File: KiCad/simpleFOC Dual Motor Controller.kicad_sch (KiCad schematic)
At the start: 15 parts, among them J101 Conn_01x04, U101 STM32F103C8Tx, U102 XT60H-M

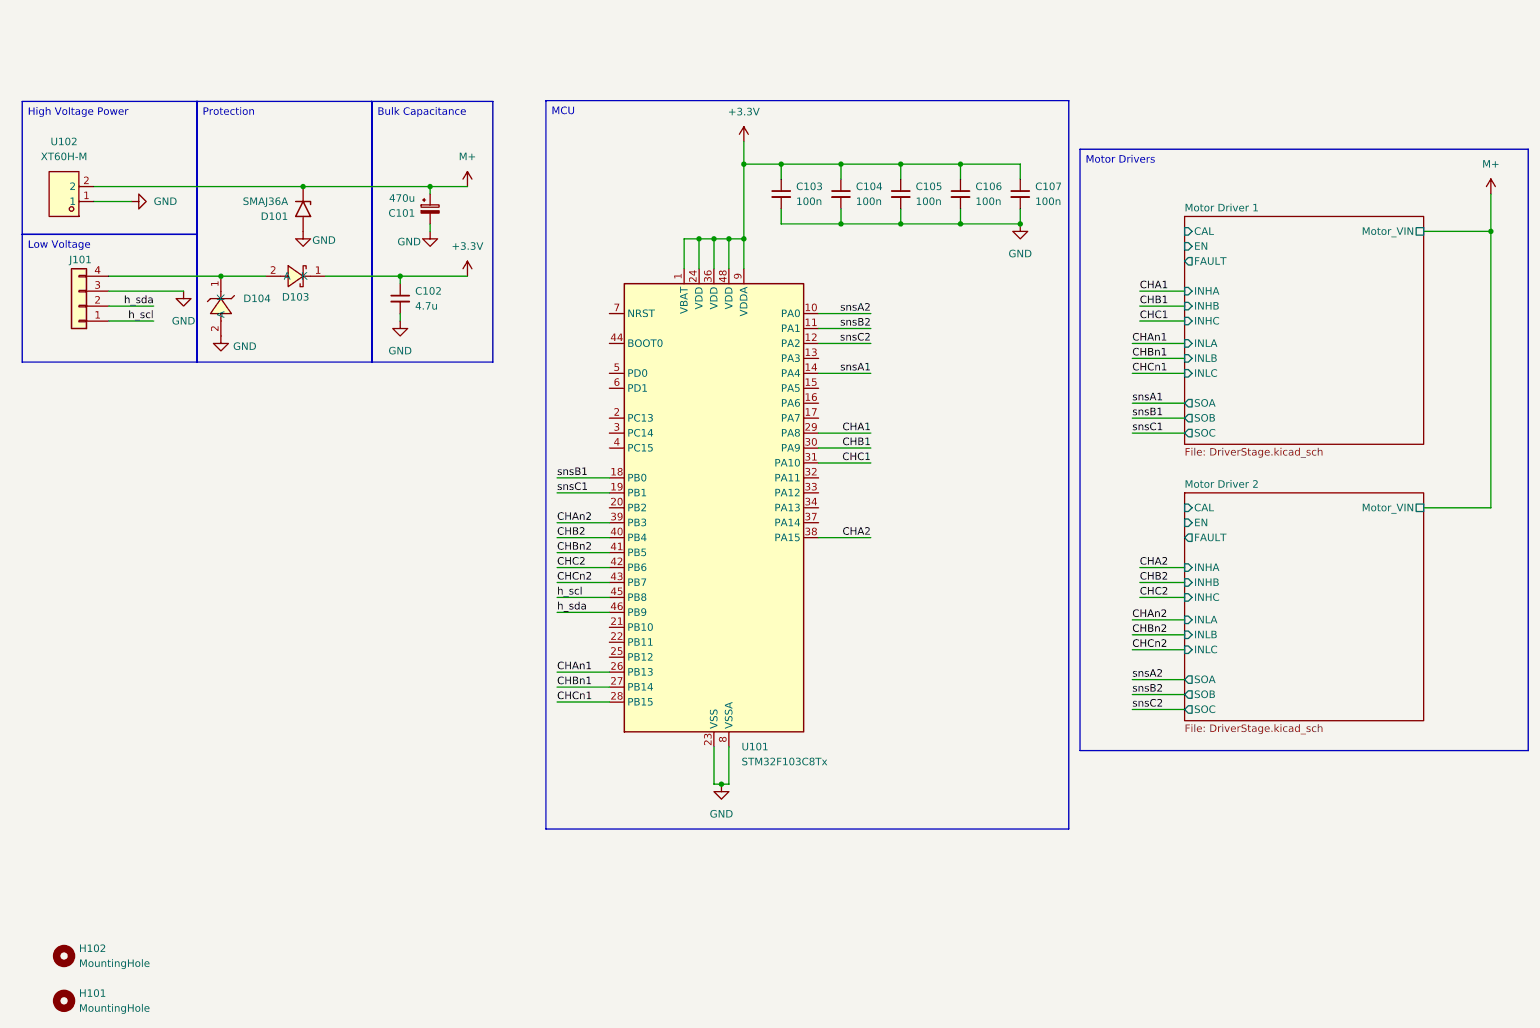
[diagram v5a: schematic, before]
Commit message: connected all control pins
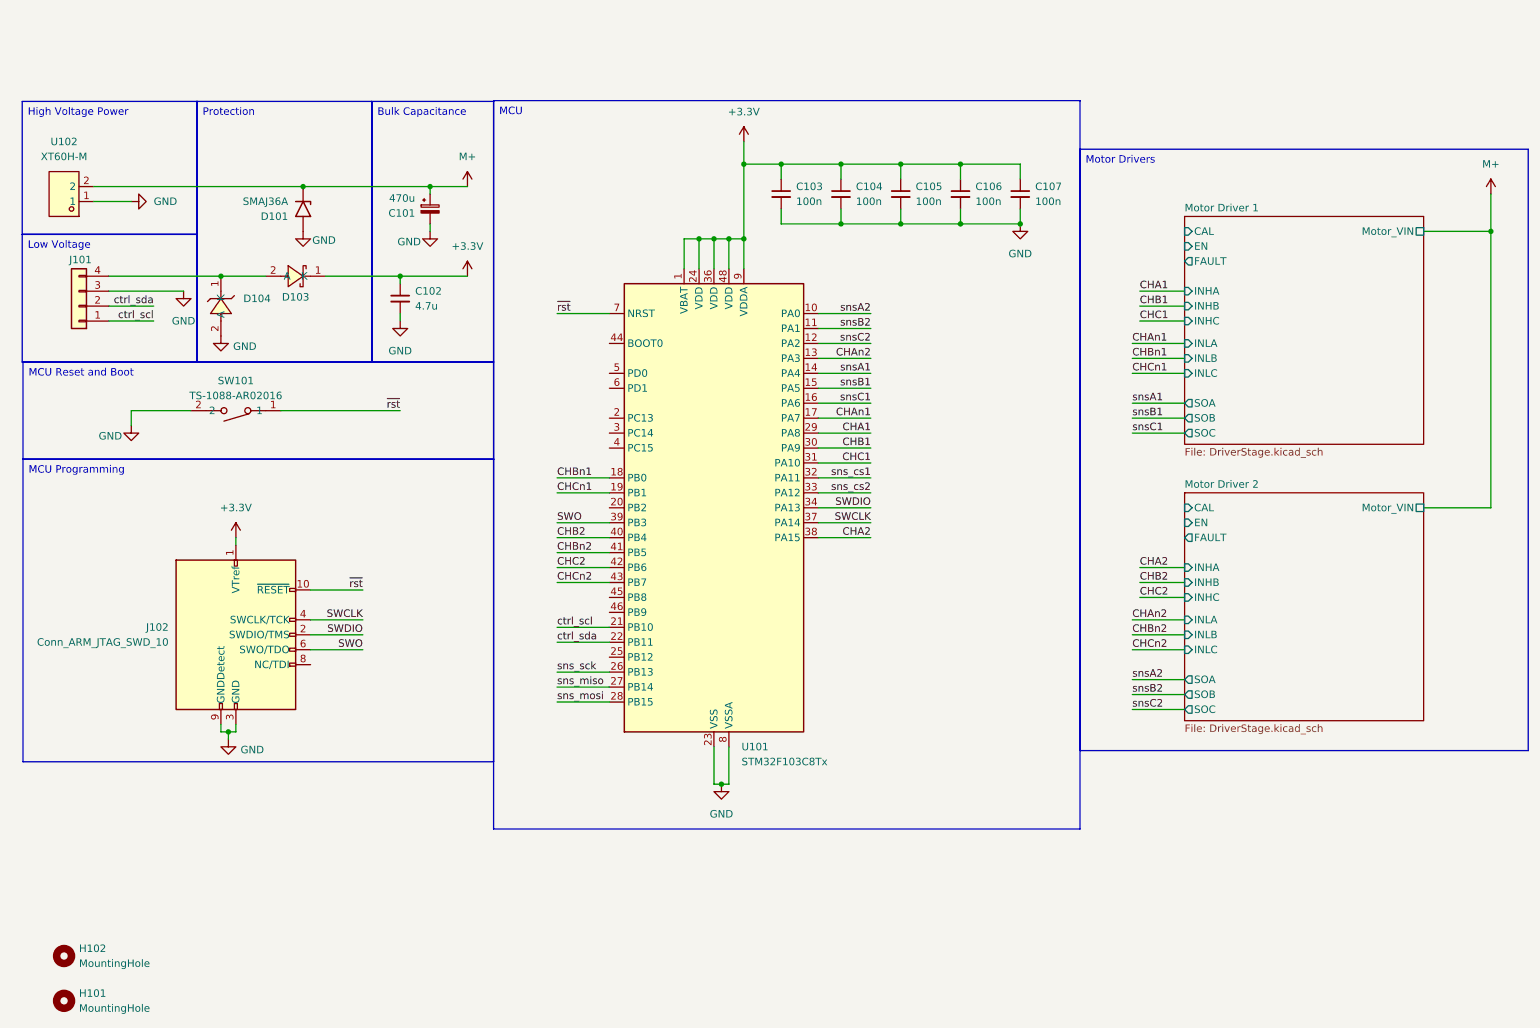
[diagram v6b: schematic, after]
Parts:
- added J102: Conn_ARM_JTAG_SWD_10, symbol Connector:Conn_ARM_JTAG_SWD_10
- added SW101: TS-1088-AR02016, easyeda2kicad:SW-SMD_L3.9-W3.0-P4.45, symbol easyeda2kicad:TS-1088-AR02016
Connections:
- net +3.3V: now also J102.1 (VTref)
- net CHAn1: now also U101.17 (PA7); no longer U101.26 (PB13)
- net CHAn2: now also U101.13 (PA3); no longer U101.39 (PB3)
- net CHBn1: now also U101.18 (PB0); no longer U101.27 (PB14)
- net CHCn1: now also U101.19 (PB1); no longer U101.28 (PB15)
- net GND: now also J102.3 (GND), J102.5 (GND), J102.9 (GNDDetect), SW101.2
- net snsB1: now also U101.15 (PA5); no longer U101.18 (PB0)
- net snsC1: now also U101.16 (PA6); no longer U101.19 (PB1)
- net ctrl_scl: now reaches U101.21 (PB10)
- net ctrl_scl: now also J101.1 (Pin_1)
- net ctrl_sda: now reaches U101.22 (PB11)
- net ctrl_sda: now also J101.2 (Pin_2)
- net sns_cs1: now reaches U101.32 (PA11)
- net sns_cs2: now reaches U101.33 (PA12)
- net SWDIO: now reaches U101.34 (PA13)
- net SWDIO: now also J102.2 (SWDIO/TMS)
- net SWCLK: now reaches U101.37 (PA14)
- net SWCLK: now also J102.4 (SWCLK/TCK)
- net ~{rst}: now reaches U101.7 (NRST)
- net ~{rst}: now also J102.10 (~{RESET}), SW101.1
- net h_scl: no longer names the net of U101.45 (PB8)
- net h_scl: no longer J101.1 (Pin_1)
- net h_sda: no longer names the net of U101.46 (PB9)
- net h_sda: no longer J101.2 (Pin_2)
- new net SWO: J102.6 (SWO/TDO), U101.39 (PB3)
- new net sns_miso: U101.27 (PB14)
- new net sns_mosi: U101.28 (PB15)
- new net sns_sck: U101.26 (PB13)

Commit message: not sure why the schematic and pcb aren't syncing :(
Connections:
- net CHAn1: now also U101.19 (PB1); no longer U101.17 (PA7)
- net CHCn1: now also U101.17 (PA7); no longer U101.19 (PB1)
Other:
- moved on the sheet: J102
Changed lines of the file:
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@@
 	)
 	(junction
-		(at 52.07 140.97)
+		(at 55.88 137.16)
 		(diameter 0)
 		(color 0 0 0 0)
@@
 	(wire
 		(pts
-			(xy 66.04 124.46) (xy 74.93 124.46)
+			(xy 69.85 120.65) (xy 78.74 120.65)
 		)
 		(stroke
@@
 	(wire
 		(pts
+			(xy 161.29 87.63) (xy 152.4 87.63)
+		)
+		(stroke
+			(width 0)
+			(type default)
+		)
+	)
+	(wire
+		(pts
 			(xy 31.75 66.04) (xy 44.45 66.04)
 		)
@@
 	(wire
 		(pts
-			(xy 66.04 127) (xy 74.93 127)
+			(xy 69.85 123.19) (xy 78.74 123.19)
 		)
 		(stroke
@@
 	(wire
 		(pts
-			(xy 50.8 140.97) (xy 52.07 140.97)
+			(xy 54.61 137.16) (xy 55.88 137.16)
 		)
 		(stroke
@@
 	(wire
 		(pts
-			(xy 66.04 116.84) (xy 74.93 116.84)
+			(xy 69.85 113.03) (xy 78.74 113.03)
 		)
 		(stroke
@@
 	(wire
 		(pts
-			(xy 53.34 139.7) (xy 53.34 140.97)
+			(xy 57.15 135.89) (xy 57.15 137.16)
 		)
 		(stroke
@@
 	(wire
 		(pts
-			(xy 66.04 121.92) (xy 74.93 121.92)
+			(xy 69.85 118.11) (xy 78.74 118.11)
 		)
 		(stroke
@@
 	(wire
 		(pts
-			(xy 161.29 87.63) (xy 152.4 87.63)
-		)
-		(stroke
-			(width 0)
-			(type default)
-		)
-	)
-	(wire
-		(pts
 			(xy 152.4 77.47) (xy 161.29 77.47)
 		)
@@
 	(wire
 		(pts
-			(xy 53.34 140.97) (xy 52.07 140.97)
+			(xy 57.15 137.16) (xy 55.88 137.16)
 		)
 		(stroke
@@
 	(wire
 		(pts
-			(xy 132.08 57.15) (xy 132.08 62.23)
+			(xy 107.95 100.33) (xy 116.84 100.33)
 		)
 		(stroke
@@
 	(wire
 		(pts
-			(xy 31.75 68.58) (xy 39.37 68.58)
+			(xy 132.08 57.15) (xy 132.08 62.23)
 		)
 		(stroke
@@
 	(wire
 		(pts
-			(xy 107.95 133.35) (xy 116.84 133.35)
+			(xy 31.75 68.58) (xy 39.37 68.58)
 		)
 		(stroke
@@
 	(wire
 		(pts
-			(xy 116.84 115.57) (xy 107.95 115.57)
+			(xy 107.95 133.35) (xy 116.84 133.35)
 		)
 		(stroke
@@
 	(wire
 		(pts
-			(xy 139.7 40.64) (xy 139.7 44.45)
+			(xy 116.84 115.57) (xy 107.95 115.57)
 		)
 		(stroke
@@
 	(wire
 		(pts
-			(xy 205.74 77.47) (xy 214.63 77.47)
+			(xy 139.7 40.64) (xy 139.7 44.45)
 		)
 		(stroke
@@
 	(wire
 		(pts
-			(xy 214.63 113.03) (xy 207.01 113.03)
+			(xy 205.74 77.47) (xy 214.63 77.47)
 		)
 		(stroke
@@
 	(wire
 		(pts
-			(xy 107.95 100.33) (xy 116.84 100.33)
+			(xy 214.63 113.03) (xy 207.01 113.03)
 		)
 		(stroke
@@
 	(wire
 		(pts
-			(xy 50.8 139.7) (xy 50.8 140.97)
+			(xy 54.61 135.89) (xy 54.61 137.16)
 		)
 		(stroke
@@
 	(wire
 		(pts
-			(xy 52.07 140.97) (xy 52.07 142.24)
+			(xy 55.88 137.16) (xy 55.88 138.43)
 		)
 		(stroke
@@
 	(wire
 		(pts
-			(xy 53.34 107.95) (xy 53.34 109.22)
+			(xy 57.15 104.14) (xy 57.15 105.41)
 		)
 		(stroke
@@
 		)
 	)
-	(label "sns_cs2"
-		(at 161.29 100.33 180)
+	(label "CHCn1"
+		(at 161.29 87.63 180)
 		(effects
 			(font
@@
 		)
 	)
-	(label "CHB1"
-		(at 161.29 92.71 180)
+	(label "sns_cs2"
+		(at 161.29 100.33 180)
 		(effects
 			(font
@@
 		)
 	)
-	(label "CHCn1"
-		(at 107.95 100.33 0)
+	(label "CHB1"
+		(at 161.29 92.71 180)
 		(effects
 			(font
 				(size 1.27 1.27)
 			)
-			(justify left bottom)
+			(justify right bottom)
 		)
 	)
@@
 	)
 	(label "SWO"
-		(at 74.93 127 180)
-		(effects
-			(font
-				(size 1.27 1.27)
-			)
-			(justify right bottom)
-		)
-	)
-	(label "CHAn1"
-		(at 161.29 87.63 180)
+		(at 78.74 123.19 180)
 		(effects
 			(font
@@
 	)
 	(label "SWCLK"
-		(at 74.93 121.92 180)
+		(at 78.74 118.11 180)
 		(effects
 			(font
@@
 		)
 	)
+	(label "CHAn1"
+		(at 107.95 100.33 0)
+		(effects
+			(font
+				(size 1.27 1.27)
+			)
+			(justify left bottom)
+		)
+	)
 	(label "CHBn2"
 		(at 205.74 124.46 0)
@@
 	)
 	(label "SWDIO"
-		(at 74.93 124.46 180)
+		(at 78.74 120.65 180)
 		(effects
 			(font
@@
 	)
 	(label "~{rst}"
-		(at 74.93 116.84 180)
+		(at 78.74 113.03 180)
 		(effects
 			(font
@@
 	(symbol
 		(lib_id "Connector:Conn_ARM_JTAG_SWD_10")
-		(at 53.34 124.46 0)
+		(at 57.15 120.65 0)
 		(unit 1)
 		(body_style 1)
@@
 		(fields_autoplaced yes)
 		(property "Reference" "J102"
-			(at 41.91 123.1899 0)
+			(at 45.72 119.3799 0)
 			(show_name no)
 			(do_not_autoplace no)
@@
 		)
 		(property "Value" "Conn_ARM_JTAG_SWD_10"
-			(at 41.91 125.7299 0)
+			(at 45.72 121.9199 0)
 			(show_name no)
 			(do_not_autoplace no)
@@
 		)
 		(property "Footprint" ""
-			(at 53.34 124.46 0)
+			(at 57.15 120.65 0)
 			(hide yes)
 			(show_name no)
@@
 		)
 		(property "Datasheet" "http://infocenter.arm.com/help/topic/com.arm.doc.ddi0314h/DDI0314H_coresight_components_trm.pdf"
-			(at 44.45 156.21 90)
+			(at 48.26 152.4 90)
 			(hide yes)
 			(show_name no)
@@
 		)
 		(property "Description" "Cortex Debug Connector, standard ARM Cortex-M SWD and JTAG interface"
-			(at 53.34 124.46 0)
+			(at 57.15 120.65 0)
 			(hide yes)
 			(show_name no)
@@
 	(symbol
 		(lib_id "power:GND")
-		(at 52.07 142.24 0)
+		(at 55.88 138.43 0)
 		(unit 1)
 		(body_style 1)
@@
 		(dnp no)
 		(property "Reference" "#PWR0119"
-			(at 52.07 148.59 0)
+			(at 55.88 144.78 0)
 			(hide yes)
 			(show_name no)
@@
 		)
 		(property "Value" "GND"
-			(at 56.134 144.018 0)
+			(at 59.944 140.208 0)
 			(show_name no)
 			(do_not_autoplace no)
@@
 		)
 		(property "Footprint" ""
-			(at 52.07 142.24 0)
+			(at 55.88 138.43 0)
 			(hide yes)
 			(show_name no)
@@
 		)
 		(property "Datasheet" ""
-			(at 52.07 142.24 0)
+			(at 55.88 138.43 0)
 			(hide yes)
 			(show_name no)
@@
 		)
 		(property "Description" "Power symbol creates a global label with name \"GND\" , ground"
-			(at 52.07 142.24 0)
+			(at 55.88 138.43 0)
 			(hide yes)
 			(show_name no)
@@
 	(symbol
 		(lib_id "power:+3.3V")
-		(at 53.34 107.95 0)
+		(at 57.15 104.14 0)
 		(unit 1)
 		(body_style 1)
@@
 		(fields_autoplaced yes)
 		(property "Reference" "#PWR0116"
-			(at 53.34 111.76 0)
+			(at 57.15 107.95 0)
 			(hide yes)
 			(show_name no)
@@
 		)
 		(property "Value" "+3.3V"
-			(at 53.34 102.87 0)
+			(at 57.15 99.06 0)
 			(show_name no)
 			(do_not_autoplace no)
@@
 		)
 		(property "Footprint" ""
-			(at 53.34 107.95 0)
+			(at 57.15 104.14 0)
 			(hide yes)
 			(show_name no)
@@
 		)
 		(property "Datasheet" ""
-			(at 53.34 107.95 0)
+			(at 57.15 104.14 0)
 			(hide yes)
 			(show_name no)
@@
 		)
 		(property "Description" "Power symbol creates a global label with name \"+3.3V\""
-			(at 53.34 107.95 0)
+			(at 57.15 104.14 0)
 			(hide yes)
 			(show_name no)

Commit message: connected a few more signals
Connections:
- net FAULT1: now reaches U101.25 (PB12)
- net FAULT2: now reaches U101.3 (PC14)
- net EN1: now reaches U101.45 (PB8)
- net CAL1: now reaches U101.46 (PB9)
- net EN2: now reaches U101.5 (PD0)
- net CAL2: now reaches U101.6 (PD1)
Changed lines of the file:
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@@
+	(wire
+		(pts
+			(xy 116.84 82.55) (xy 107.95 82.55)
+		)
+		(stroke
+			(width 0)
+			(type default)
+		)
+	)
 	(wire
 		(pts
@@
 	(wire
 		(pts
+			(xy 214.63 55.88) (xy 205.74 55.88)
+		)
+		(stroke
+			(width 0)
+			(type default)
+		)
+	)
+	(wire
+		(pts
 			(xy 166.37 54.61) (xy 176.53 54.61)
 		)
@@
 	(wire
 		(pts
-			(xy 214.63 68.58) (xy 207.01 68.58)
+			(xy 214.63 68.58) (xy 205.74 68.58)
 		)
 		(stroke
@@
 	(wire
 		(pts
-			(xy 214.63 71.12) (xy 207.01 71.12)
+			(xy 214.63 71.12) (xy 205.74 71.12)
+		)
+		(stroke
+			(width 0)
+			(type default)
+		)
+	)
+	(wire
+		(pts
+			(xy 214.63 107.95) (xy 205.74 107.95)
 		)
 		(stroke
@@
 	(wire
 		(pts
+			(xy 214.63 102.87) (xy 205.74 102.87)
+		)
+		(stroke
+			(width 0)
+			(type default)
+		)
+	)
+	(wire
+		(pts
 			(xy 137.16 143.51) (xy 137.16 149.86)
 		)
@@
 	(wire
 		(pts
+			(xy 116.84 120.65) (xy 107.95 120.65)
+		)
+		(stroke
+			(width 0)
+			(type default)
+		)
+	)
+	(wire
+		(pts
 			(xy 205.74 74.93) (xy 214.63 74.93)
 		)
@@
 	(wire
 		(pts
+			(xy 116.84 128.27) (xy 107.95 128.27)
+		)
+		(stroke
+			(width 0)
+			(type default)
+		)
+	)
+	(wire
+		(pts
 			(xy 86.36 49.53) (xy 86.36 48.26)
 		)
@@
 	(wire
 		(pts
+			(xy 214.63 58.42) (xy 205.74 58.42)
+		)
+		(stroke
+			(width 0)
+			(type default)
+		)
+	)
+	(wire
+		(pts
 			(xy 57.15 135.89) (xy 57.15 137.16)
 		)
@@
 	(wire
 		(pts
-			(xy 214.63 66.04) (xy 207.01 66.04)
+			(xy 214.63 66.04) (xy 205.74 66.04)
 		)
 		(stroke
@@
 	(wire
 		(pts
+			(xy 214.63 105.41) (xy 205.74 105.41)
+		)
+		(stroke
+			(width 0)
+			(type default)
+		)
+	)
+	(wire
+		(pts
 			(xy 57.15 137.16) (xy 55.88 137.16)
 		)
@@
 	(wire
 		(pts
+			(xy 116.84 90.17) (xy 107.95 90.17)
+		)
+		(stroke
+			(width 0)
+			(type default)
+		)
+	)
+	(wire
+		(pts
 			(xy 132.08 57.15) (xy 132.08 62.23)
 		)
@@
 	(wire
 		(pts
+			(xy 116.84 80.01) (xy 107.95 80.01)
+		)
+		(stroke
+			(width 0)
+			(type default)
+		)
+	)
+	(wire
+		(pts
 			(xy 116.84 105.41) (xy 107.95 105.41)
 		)
@@
 	(wire
 		(pts
+			(xy 214.63 60.96) (xy 205.74 60.96)
+		)
+		(stroke
+			(width 0)
+			(type default)
+		)
+	)
+	(wire
+		(pts
 			(xy 35.56 86.36) (xy 45.72 86.36)
+		)
+		(stroke
+			(width 0)
+			(type default)
+		)
+	)
+	(wire
+		(pts
+			(xy 116.84 118.11) (xy 107.95 118.11)
 		)
 		(stroke
@@
 		)
 	)
+	(label "CAL1"
+		(at 205.74 55.88 0)
+		(effects
+			(font
+				(size 1.27 1.27)
+			)
+			(justify left bottom)
+		)
+	)
 	(label "CHA2"
 		(at 161.29 107.95 180)
@@
 		)
 	)
+	(label "FAULT1"
+		(at 107.95 128.27 0)
+		(effects
+			(font
+				(size 1.27 1.27)
+			)
+			(justify left bottom)
+		)
+	)
+	(label "CAL2"
+		(at 107.95 82.55 0)
+		(effects
+			(font
+				(size 1.27 1.27)
+			)
+			(justify left bottom)
+		)
+	)
 	(label "CHCn1"
 		(at 161.29 87.63 180)
@@
 		)
 	)
+	(label "FAULT2"
+		(at 107.95 90.17 0)
+		(effects
+			(font
+				(size 1.27 1.27)
+			)
+			(justify left bottom)
+		)
+	)
 	(label "CHA1"
 		(at 161.29 90.17 180)
@@
 		)
 	)
+	(label "FAULT2"
+		(at 205.74 107.95 0)
+		(effects
+			(font
+				(size 1.27 1.27)
+			)
+			(justify left bottom)
+		)
+	)
 	(label "snsB1"
 		(at 161.29 82.55 180)
@@
 	)
 	(label "CHC1"
-		(at 207.01 71.12 0)
+		(at 205.74 71.12 0)
+		(effects
+			(font
+				(size 1.27 1.27)
+			)
+			(justify left bottom)
+		)
+	)
+	(label "EN1"
+		(at 205.74 58.42 0)
+		(effects
+			(font
+				(size 1.27 1.27)
+			)
+			(justify left bottom)
+		)
+	)
+	(label "CAL1"
+		(at 107.95 120.65 0)
 		(effects
 			(font
@@
 	)
 	(label "CHA1"
-		(at 207.01 66.04 0)
+		(at 205.74 66.04 0)
 		(effects
 			(font
@@
 		)
 	)
+	(label "EN1"
+		(at 107.95 118.11 0)
+		(effects
+			(font
+				(size 1.27 1.27)
+			)
+			(justify left bottom)
+		)
+	)
 	(label "CHAn2"
 		(at 205.74 121.92 0)
@@
 		)
 	)
+	(label "EN2"
+		(at 107.95 80.01 0)
+		(effects
+			(font
+				(size 1.27 1.27)
+			)
+			(justify left bottom)
+		)
+	)
 	(label "SWCLK"
 		(at 161.29 105.41 180)
@@
 		)
 	)
+	(label "CAL2"
+		(at 205.74 102.87 0)
+		(effects
+			(font
+				(size 1.27 1.27)
+			)
+			(justify left bottom)
+		)
+	)
 	(label "SWCLK"
 		(at 78.74 118.11 180)
@@
 		)
 	)
+	(label "FAULT1"
+		(at 205.74 60.96 0)
+		(effects
+			(font
+				(size 1.27 1.27)
+			)
+			(justify left bottom)
+		)
+	)
 	(label "ctrl_sda"
 		(at 107.95 125.73 0)
@@
 		)
 	)
+	(label "EN2"
+		(at 205.74 105.41 0)
+		(effects
+			(font
+				(size 1.27 1.27)
+			)
+			(justify left bottom)
+		)
+	)
 	(label "snsB2"
 		(at 161.29 72.39 180)
@@
 	)
 	(label "CHB1"
-		(at 207.01 68.58 0)
-		(effects
-			(font
+		(at 205.74 68.58 0)
+		(effects
+			(font
